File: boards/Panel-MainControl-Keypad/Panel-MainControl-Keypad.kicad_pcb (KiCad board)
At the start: 2 copper layers, 142 x 72 mm, 29 parts, among them J1 Conn_01x10, J2 Conn_01x10, SW1 SW_Push, SW10 SW_Push, SW11 RotaryEncoder_Switch, SW12 RotaryEncoder_Switch, SW2 SW_Push, SW3 SW_Push, SW4 SW_Push, SW5 SW_Push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

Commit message: Updated LED resistor values
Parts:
- R1, R2: value 220 -> 150
- R3: value 220 -> 470
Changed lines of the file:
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@@
 			)
 		)
-		(property "Value" "220"
+		(property "Value" "150"
 			(at 5.08 2.37 90)
 			(layer "F.Fab")
@@
 		)
 		(fp_text user "${REFERENCE}"
-			(at 2 2.5 360)
+			(at 2 2.5 0)
 			(layer "F.Fab")
 			(effects
@@
 			)
 		)
-		(property "Value" "220"
+		(property "Value" "150"
 			(at 5.08 2.37 90)
 			(layer "F.Fab")
@@
 		)
 		(fp_text user "${REFERENCE}"
-			(at 2 2.5 360)
+			(at 2 2.5 0)
 			(layer "F.Fab")
 			(effects
@@
 		)
 		(fp_text user "${REFERENCE}"
-			(at 0 9 360)
+			(at 0 9 0)
 			(layer "F.Fab")
 			(effects
@@
 			)
 		)
-		(property "Value" "220"
+		(property "Value" "470"
 			(at 5.08 2.37 90)
 			(layer "F.Fab")
@@
 		)
 		(fp_text user "${REFERENCE}"
-			(at 0 9 360)
+			(at 0 9 0)
 			(layer "F.Fab")
 			(effects

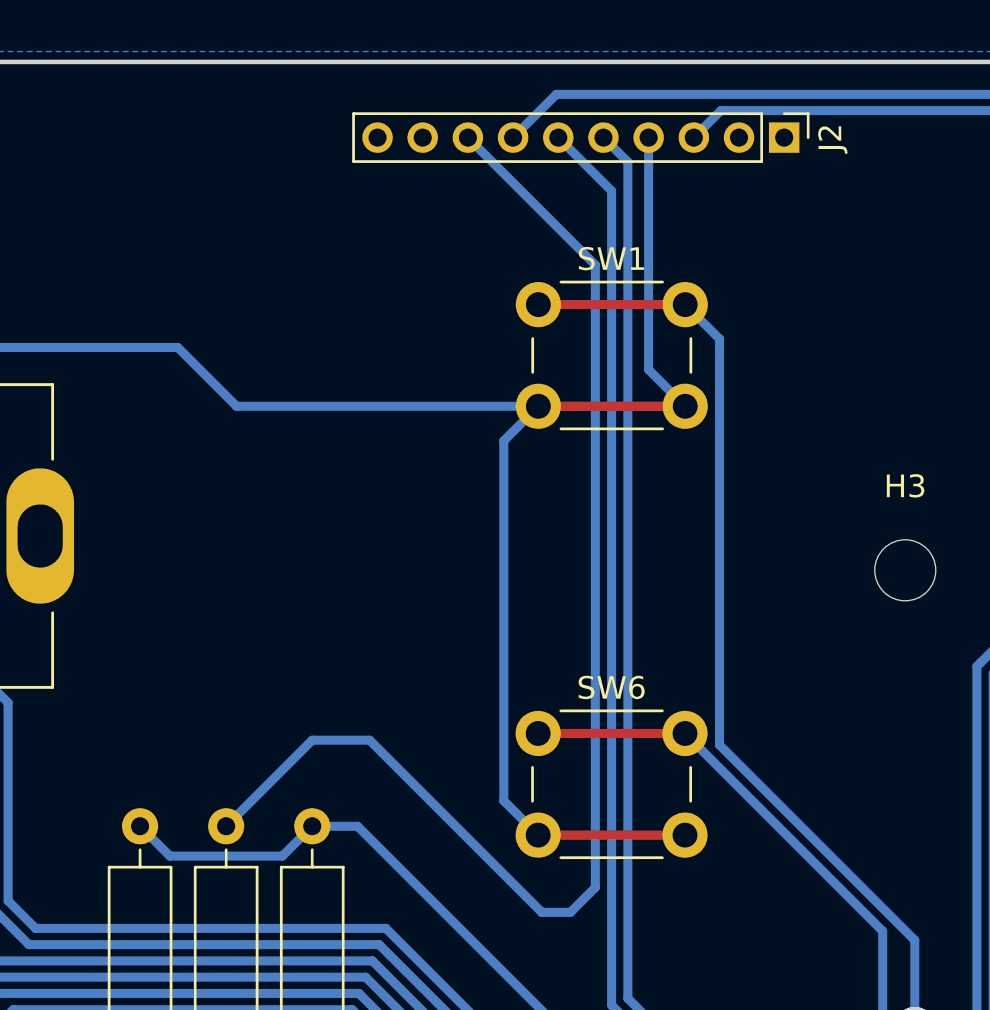
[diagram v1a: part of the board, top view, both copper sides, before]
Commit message: Fixed using 5V from main power for PWR LED
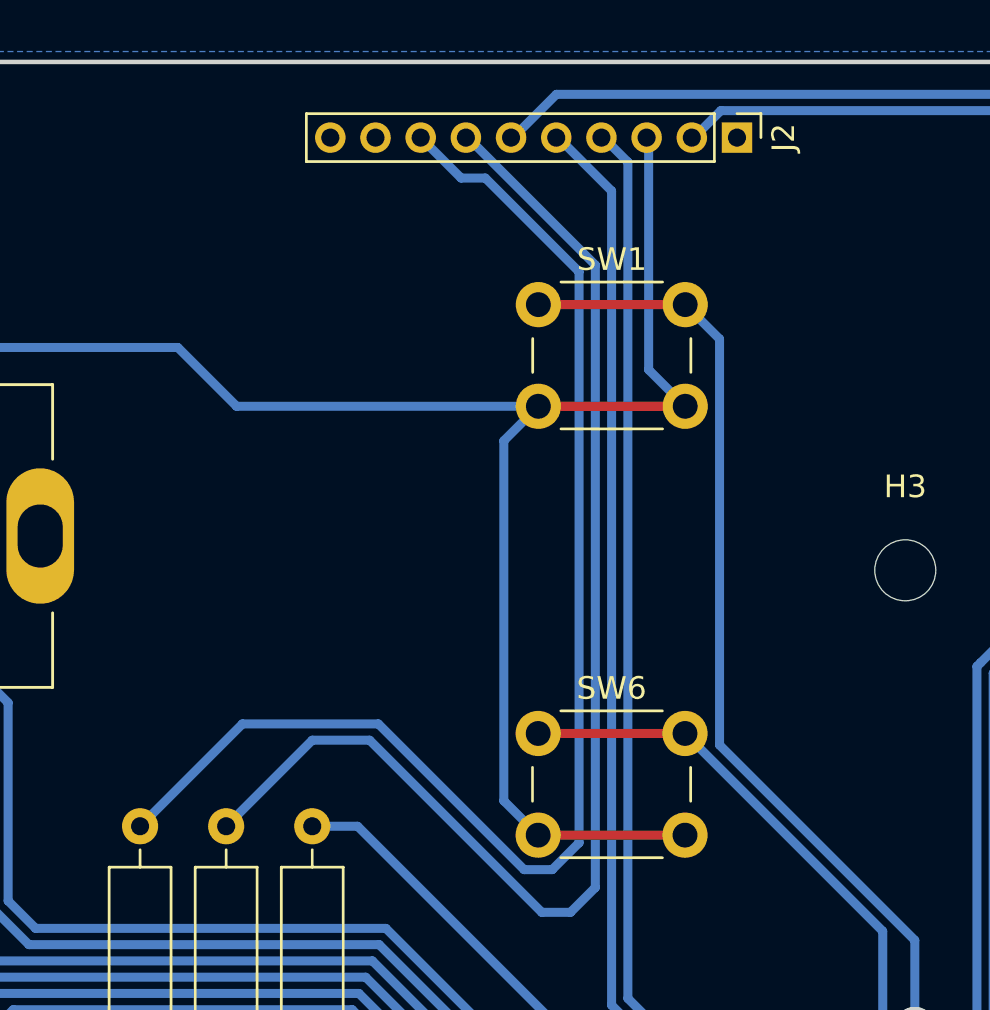
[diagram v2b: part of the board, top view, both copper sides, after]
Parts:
- moved J2 2.09 mm to (126.8, 69.8)
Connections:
- J2 pad 2: unconnected-(J2-Pin_2-Pad2) -> /KP_Line2
- J2 pad 3: /KP_Line2 -> /KP_Line3
- J2 pad 4: /KP_Line3 -> /FX2
- J2 pad 5: /FX2 -> /FX1
- J2 pad 6: /FX1 -> /LED_Ctrl
- J2 pad 7: /LED_Ctrl -> +12V
- J2 pad 8: +12V -> +5VA
- R2 pad 2: +5V -> +5VA
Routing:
- net +5VA: track 0.00 -> 59.2 mm
- net +5V: track 221.1 -> 212.3 mm
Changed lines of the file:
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@@
 	(net 24 "/A1")
 	(net 25 "unconnected-(J2-Pin_1-Pad1)")
-	(net 26 "unconnected-(J2-Pin_2-Pad2)")
+	(net 26 "+5VA")
 	(footprint "Button_Switch_THT:SW_PUSH_6mm_H9.5mm"
 		(layer "F.Cu")
@@
 			(layers "*.Cu" "*.Mask")
 			(remove_unused_layers no)
-			(net 4 "+5V")
+			(net 26 "+5VA")
 			(pintype "passive")
 		)
@@
 	(footprint "Connector_PinHeader_2.00mm:PinHeader_1x10_P2.00mm_Vertical"
 		(layer "F.Cu")
-		(at 128.84 69.85 -90)
+		(at 126.75 69.85 -90)
 		(descr "Through hole straight pin header, 1x10, 2.00mm pitch, single row")
 		(tags "Through hole pin header THT 1x10 2.00mm single row")
@@
 			(layers "*.Cu" "*.Mask")
 			(remove_unused_layers no)
-			(net 26 "unconnected-(J2-Pin_2-Pad2)")
+			(net 19 "/KP_Line2")
 			(pinfunction "Pin_2")
-			(pintype "passive+no_connect")
+			(pintype "passive")
 		)
 		(pad "3" thru_hole oval
@@
 			(layers "*.Cu" "*.Mask")
 			(remove_unused_layers no)
-			(net 19 "/KP_Line2")
+			(net 13 "/KP_Line3")
 			(pinfunction "Pin_3")
 			(pintype "passive")
@@
 			(layers "*.Cu" "*.Mask")
 			(remove_unused_layers no)
-			(net 13 "/KP_Line3")
+			(net 6 "/FX2")
 			(pinfunction "Pin_4")
 			(pintype "passive")
@@
 			(layers "*.Cu" "*.Mask")
 			(remove_unused_layers no)
-			(net 6 "/FX2")
+			(net 2 "/FX1")
 			(pinfunction "Pin_5")
 			(pintype "passive")
@@
 			(layers "*.Cu" "*.Mask")
 			(remove_unused_layers no)
-			(net 2 "/FX1")
+			(net 20 "/LED_Ctrl")
 			(pinfunction "Pin_6")
 			(pintype "passive")
@@
 			(layers "*.Cu" "*.Mask")
 			(remove_unused_layers no)
-			(net 20 "/LED_Ctrl")
+			(net 11 "+12V")
 			(pinfunction "Pin_7")
 			(pintype "passive")
@@
 			(layers "*.Cu" "*.Mask")
 			(remove_unused_layers no)
-			(net 11 "+12V")
+			(net 26 "+5VA")
 			(pinfunction "Pin_8")
 			(pintype "passive")
@@
 	)
 	(segment
-		(start 100.33 100.33)
-		(end 101.65 101.65)
-		(width 0.4)
-		(layer "B.Cu")
-		(net 4)
-	)
-	(segment
 		(start 199.272329 106.68)
 		(end 173.074714 106.68)
@@
 	)
 	(segment
-		(start 106.63 101.65)
-		(end 107.95 100.33)
-		(width 0.4)
-		(layer "B.Cu")
-		(net 4)
-	)
-	(segment
 		(start 206.892329 99.06)
 		(end 207.01 99.06)
@@
 	)
 	(segment
-		(start 101.65 101.65)
-		(end 106.63 101.65)
-		(width 0.4)
-		(layer "B.Cu")
-		(net 4)
-	)
-	(segment
 		(start 122.168184 112.54)
 		(end 128.42 112.54)
@@
 		(net 24)
 	)
+	(segment
+		(start 117.326765 102.25)
+		(end 118.572153 102.25)
+		(width 0.4)
+		(layer "B.Cu")
+		(net 26)
+	)
+	(segment
+		(start 119.76 75.788234)
+		(end 115.610883 71.639117)
+		(width 0.4)
+		(layer "B.Cu")
+		(net 26)
+	)
+	(segment
+		(start 119.76 101.062153)
+		(end 119.76 75.788234)
+		(width 0.4)
+		(layer "B.Cu")
+		(net 26)
+	)
+	(segment
+		(start 118.572153 102.25)
+		(end 119.76 101.062153)
+		(width 0.4)
+		(layer "B.Cu")
+		(net 26)
+	)
+	(segment
+		(start 100.33 100.33)
+		(end 104.86 95.8)
+		(width 0.4)
+		(layer "B.Cu")
+		(net 26)
+	)
+	(segment
+		(start 104.86 95.8)
+		(end 110.876765 95.8)
+		(width 0.4)
+		(layer "B.Cu")
+		(net 26)
+	)
+	(segment
+		(start 115.610883 71.639117)
+		(end 114.539117 71.639117)
+		(width 0.4)
+		(layer "B.Cu")
+		(net 26)
+	)
+	(segment
+		(start 114.539117 71.639117)
+		(end 112.75 69.85)
+		(width 0.4)
+		(layer "B.Cu")
+		(net 26)
+	)
+	(segment
+		(start 110.876765 95.8)
+		(end 117.326765 102.25)
+		(width 0.4)
+		(layer "B.Cu")
+		(net 26)
+	)
 	(zone
